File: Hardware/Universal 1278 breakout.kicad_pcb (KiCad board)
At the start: 2 copper layers, 26.7 x 30.6 mm, 7 parts, among them J1 Conn_Coaxial, J2 Conn_01x10, J3 Conn_01x10, U2 DRF1278F

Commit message: Various updates.
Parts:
- J1: footprint Connector_Coaxial:SMA_Molex_73251-2120_EdgeMount_Horizontal -> My footprints:SMA_EdgeMount_Holes
- moved J1 0.07 mm to (155.5, 81.4), turned to 180 degrees
- renumbered XL2178-SMT to U1
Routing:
- net (no net): track 2.54 -> 0.00 mm
- net DIO5: track 46.6 -> 48.1 mm
- net DIO4: track 41.2 -> 42.7 mm
- net RESET: track 36.2 -> 37.3 mm
- net GND: track 17.0 -> 15.9 mm, vias 26 -> 42
- net DIO1: track 30.7 -> 31.4 mm
- net DIO2: track 28.0 -> 28.6 mm
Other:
- board text added: "MBB LoRa DRF1278F/ XL1278-SMT BB v1.0 git.io/JtAfU"
- board text removed: "TODO: * U.FL etc. footprint with holes for ANT * Groundplane * Another set of 0.05" holes to adapt XL1278-SMT to DRF1278F with 0.05" pins?"

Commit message: Update.
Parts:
- J1: footprint My footprints:SMA_EdgeMount_Holes -> Misc RF:SMA_EdgeMount_Holes
- U1: footprint My footprints:XL1278-SMT -> Misc RF:XL1278-SMT
- U2: footprint My footprints:DRF1278F -> Misc RF:DRF1278F
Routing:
- net GND: track 15.9 -> 29.9 mm

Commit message: Further updates
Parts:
- removed JP1: SolderJumper_3_Open, Jumper:SolderJumper-3_P1.3mm_Open_RoundedPad1.0x1.5mm
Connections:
- U1 pad 16: Net-(JP1-Pad3) -> Net-(J1-Pad1)
- U2 pad 15: Net-(JP1-Pad1) -> Net-(J1-Pad1)
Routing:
- net Net-(J1-Pad1): track 15.3 -> 17.5 mm
- net Net-(JP1-Pad1): track 2.02 -> 0.00 mm
- net Net-(JP1-Pad3): track 1.78 -> 0.00 mm
- net DIO0: track 30.1 -> 29.1 mm
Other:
- board text added: "BB v1.0"
- board text removed: "BB v0.1"

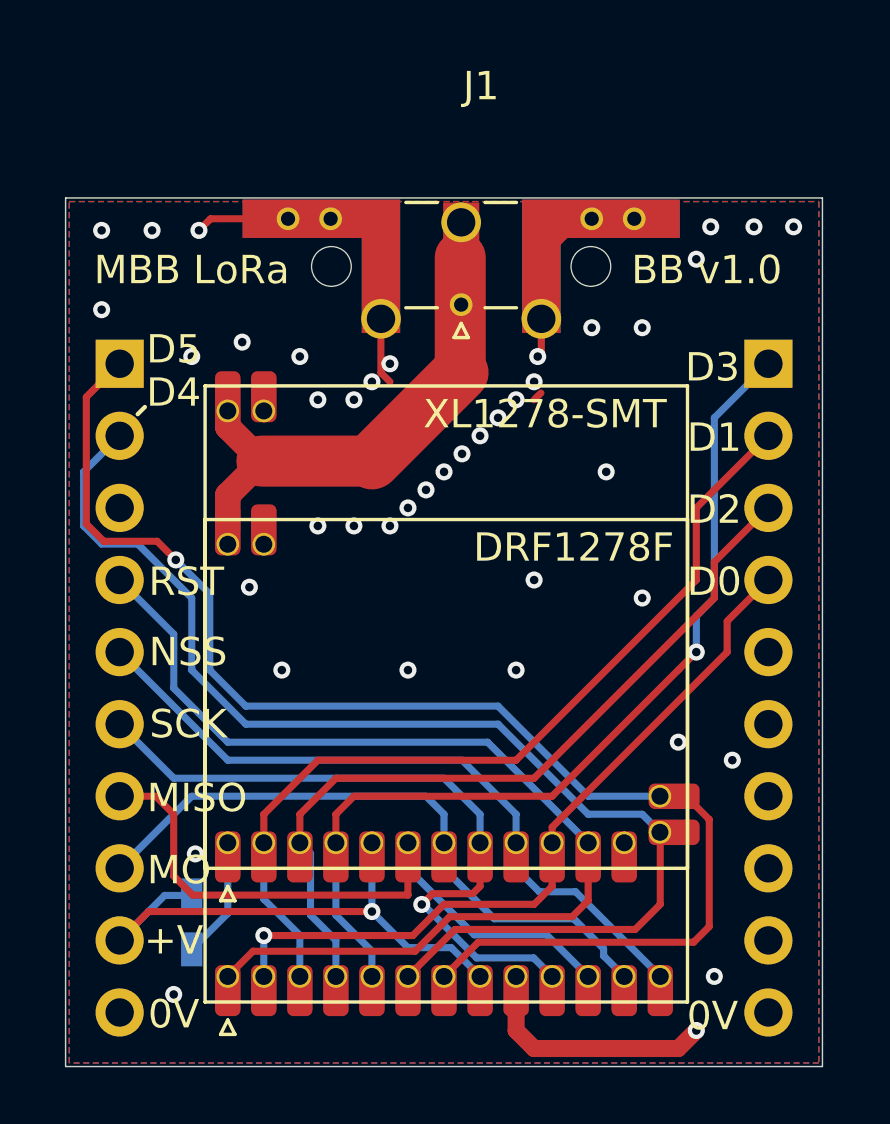
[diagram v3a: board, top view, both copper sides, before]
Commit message: Fix antenna ground connections
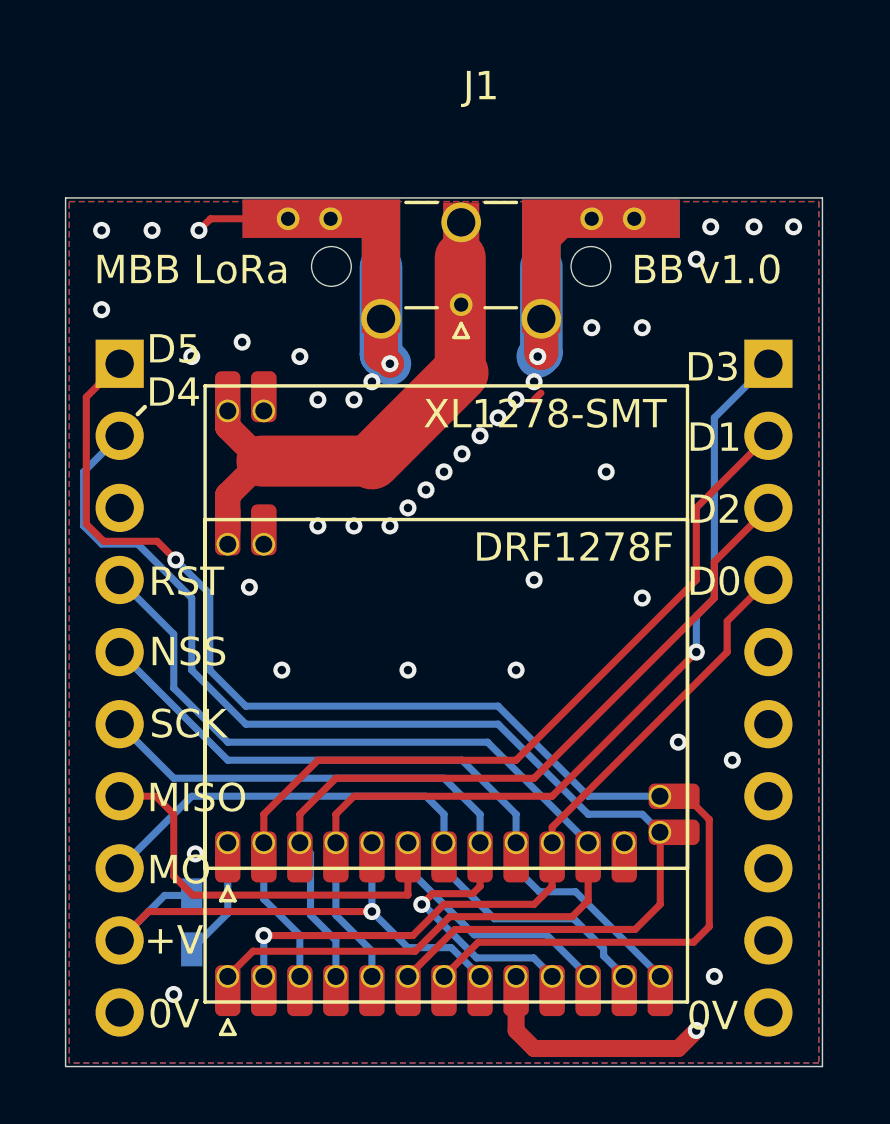
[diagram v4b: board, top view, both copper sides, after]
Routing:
- net GND: track 30.0 -> 36.2 mm
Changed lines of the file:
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@@
     (thickness 1.6002)
     (drawings 28)
-    (tracks 213)
+    (tracks 217)
     (zones 0)
     (modules 6)
@@
   )
   (setup
-    (last_trace_width 0.25)
+    (last_trace_width 1.5)
     (user_trace_width 0.15)
     (user_trace_width 0.2)
@@
     (visible_elements 7FFFFFFF)
     (pcbplotparams
-      (layerselection 0x010fc_ffffffff)
+      (layerselection 0x010f0_ffffffff)
       (usegerberextensions false)
       (usegerberattributes true)
@@
       (drillshape 0)
       (scaleselection 1)
-      (outputdirectory ""))
+      (outputdirectory "Gerbers/"))
   )
   (net 0 "")
@@
       (effects (font (size 1 1) (thickness 0.15)))
     )
-    (fp_text user %R (at 9.095 0 180) (layer F.Fab)
-      (effects (font (size 1 1) (thickness 0.15)))
-    )
-    (fp_text user "PCB Edge" (at 0.127 2.6035 180) (layer Dwgs.User)
-      (effects (font (size 0.5 0.5) (thickness 0.08)))
-    )
-    (fp_text user "Board Thickness: 1.57mm" (at 0 -5.45 180) (layer Cmts.User)
-      (effects (font (size 1 1) (thickness 0.15)))
-    )
     (fp_line (start -0.25 -2.76) (end 0 -2.26) (layer F.SilkS) (width 0.12))
     (fp_line (start 0.25 -2.76) (end -0.25 -2.76) (layer F.SilkS) (width 0.12))
@@
     (fp_line (start -1.95 -1.71) (end -0.84 -1.71) (layer F.SilkS) (width 0.12))
     (fp_line (start 0.84 -1.71) (end 1.95 -1.71) (layer F.SilkS) (width 0.12))
+    (fp_text user %R (at 9.095 0 180) (layer F.Fab)
+      (effects (font (size 1 1) (thickness 0.15)))
+    )
+    (fp_text user "PCB Edge" (at 0.127 2.6035 180) (layer Dwgs.User)
+      (effects (font (size 0.5 0.5) (thickness 0.08)))
+    )
+    (fp_text user "Board Thickness: 1.57mm" (at 0 -5.45 180) (layer Cmts.User)
+      (effects (font (size 1 1) (thickness 0.15)))
+    )
     (pad 2 smd rect (at -5.6 1.425 270) (size 1.35 4.2) (layers Back B.Mask)
       (net 2 GND))
@@
   )
   (segment (start 155.5115 81.3435) (end 155.5115 85.4075) (width 1.8) (layer Front) (net 1))
+  (segment (start 147.32 87.317685) (end 148.521315 88.519) (width 0.9) (layer Front) (net 1))
+  (segment (start 147.32 86.752) (end 147.32 87.317685) (width 0.9) (layer Front) (net 1))
+  (segment (start 147.32 89.720315) (end 147.32 90.943) (width 0.9) (layer Front) (net 1))
+  (segment (start 148.521315 88.519) (end 147.32 89.720315) (width 0.9) (layer Front) (net 1))
+  (segment (start 155.5115 85.4075) (end 152.4 88.519) (width 2) (layer Front) (net 1))
+  (segment (start 152.4 88.519) (end 148.521315 88.519) (width 1.8) (layer Front) (net 1))
   (via (at 163.83 108.585) (size 0.6) (drill 0.3) (layers Front Back) (net 2))
   (via (at 145.415 107.315) (size 0.6) (drill 0.3) (layers Front Back) (net 2))
@@
   (via (at 158.115 92.71) (size 0.6) (drill 0.3) (layers Front Back) (net 2))
   (via (at 153.67 95.885) (size 0.6) (drill 0.3) (layers Front Back) (net 2))
-  (segment (start 152.7048 81.3816) (end 152.7048 83.8708) (width 0.25) (layer Front) (net 2))
+  (segment (start 152.7048 81.3816) (end 152.7048 83.8708) (width 1.2) (layer Front) (net 2))
   (segment (start 158.3548 86.1202) (end 158.115 86.36) (width 0.25) (layer Front) (net 2))
   (via (at 164.338 80.264) (size 0.6) (drill 0.3) (layers Front Back) (net 2))
@@
   (via (at 146.177 102.362) (size 0.6) (drill 0.3) (layers Front Back) (net 2))
   (via (at 148.082 92.964) (size 0.6) (drill 0.3) (layers Front Back) (net 2))
+  (segment (start 158.369 84.709) (end 158.242 84.836) (width 0.25) (layer Front) (net 2))
+  (segment (start 158.369 81.657) (end 158.369 84.709) (width 1.2) (layer Front) (net 2))
+  (segment (start 152.719 84.774) (end 153.035 85.09) (width 1) (layer Front) (net 2))
+  (segment (start 152.719 81.657) (end 152.719 84.774) (width 1.2) (layer Front) (net 2))
+  (segment (start 158.369 84.709) (end 158.242 84.836) (width 1.5) (layer Back) (net 2))
+  (segment (start 158.369 81.657) (end 158.369 84.709) (width 1.5) (layer Back) (net 2))
+  (segment (start 152.719 84.774) (end 153.035 85.09) (width 1.5) (layer Back) (net 2))
+  (segment (start 152.719 81.657) (end 152.719 84.774) (width 1.5) (layer Back) (net 2))
   (segment (start 156.21 106.68) (end 155.194 105.664) (width 0.25) (layer Back) (net 3))
   (segment (start 155.194 105.664) (end 153.67 105.664) (width 0.25) (layer Back) (net 3))
@@
   (segment (start 148.59 103.955998) (end 149.86 105.225998) (width 0.25) (layer Back) (net 13))
   (segment (start 148.59 101.97) (end 148.59 103.955998) (width 0.25) (layer Back) (net 13))
+  (segment (start 163.83 92.71) (end 163.83 90.17) (width 0.25) (layer Front) (net 13))
+  (segment (start 157.48 99.06) (end 163.83 92.71) (width 0.25) (layer Front) (net 13))
+  (segment (start 150.495 99.06) (end 157.48 99.06) (width 0.25) (layer Front) (net 13))
+  (segment (start 148.59 100.965) (end 150.495 99.06) (width 0.25) (layer Front) (net 13))
+  (segment (start 148.59 101.97) (end 148.59 100.965) (width 0.25) (layer Front) (net 13))
+  (segment (start 163.83 90.17) (end 166.37 87.63) (width 0.25) (layer Front) (net 13))
   (segment (start 165.735 90.17) (end 166.37 90.17) (width 0.25) (layer Front) (net 14))
   (segment (start 150.237009 102.347009) (end 150.237009 104.517009) (width 0.25) (layer Back) (net 14))
@@
   (segment (start 164.918038 94.161962) (end 166.37 92.71) (width 0.25) (layer Front) (net 15))
   (segment (start 164.918038 95.25) (end 164.918038 94.161962) (width 0.25) (layer Front) (net 15))
-  (segment (start 147.32 87.317685) (end 148.521315 88.519) (width 0.9) (layer Front) (net 1))
-  (segment (start 147.32 86.752) (end 147.32 87.317685) (width 0.9) (layer Front) (net 1))
-  (segment (start 147.32 89.720315) (end 147.32 90.943) (width 0.9) (layer Front) (net 1))
-  (segment (start 148.521315 88.519) (end 147.32 89.720315) (width 0.9) (layer Front) (net 1))
-  (segment (start 155.5115 85.4075) (end 152.4 88.519) (width 2) (layer Front) (net 1))
-  (segment (start 152.4 88.519) (end 148.521315 88.519) (width 1.8) (layer Front) (net 1))
-  (segment (start 152.719 85.409) (end 153.035 85.725) (width 0.25) (layer Front) (net 2))
-  (segment (start 152.719 81.657) (end 152.719 85.409) (width 0.25) (layer Front) (net 2))
-  (segment (start 158.369 84.709) (end 158.242 84.836) (width 0.25) (layer Front) (net 2))
-  (segment (start 158.369 81.657) (end 158.369 84.709) (width 0.25) (layer Front) (net 2))
-  (segment (start 163.83 92.71) (end 163.83 90.17) (width 0.25) (layer Front) (net 13))
-  (segment (start 157.48 99.06) (end 163.83 92.71) (width 0.25) (layer Front) (net 13))
-  (segment (start 150.495 99.06) (end 157.48 99.06) (width 0.25) (layer Front) (net 13))
-  (segment (start 148.59 100.965) (end 150.495 99.06) (width 0.25) (layer Front) (net 13))
-  (segment (start 148.59 101.97) (end 148.59 100.965) (width 0.25) (layer Front) (net 13))
-  (segment (start 163.83 90.17) (end 166.37 87.63) (width 0.25) (layer Front) (net 13))
   (zone (net 2) (net_name GND) (layer Back) (hatch edge 0.508)
     (connect_pads (clearance 0.508))
@@
     (polygon
       (pts
-        (xy 157.48 84.455) (xy 153.543 84.455) (xy 153.543 79.375) (xy 157.4798 79.3816)
+        (xy 157.48 85.09) (xy 153.543 85.09) (xy 153.543 79.375) (xy 157.4798 79.3816)
       )
     )

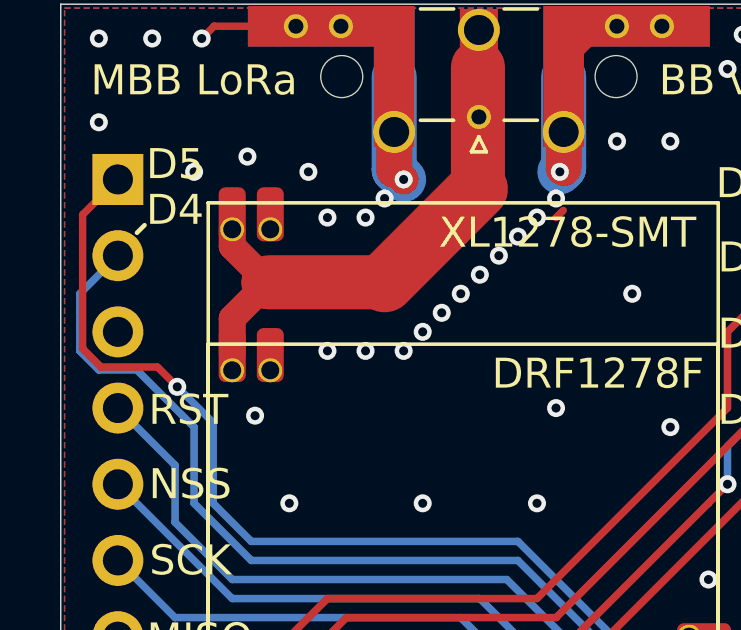
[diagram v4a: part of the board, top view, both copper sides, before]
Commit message: Fix more grounds.
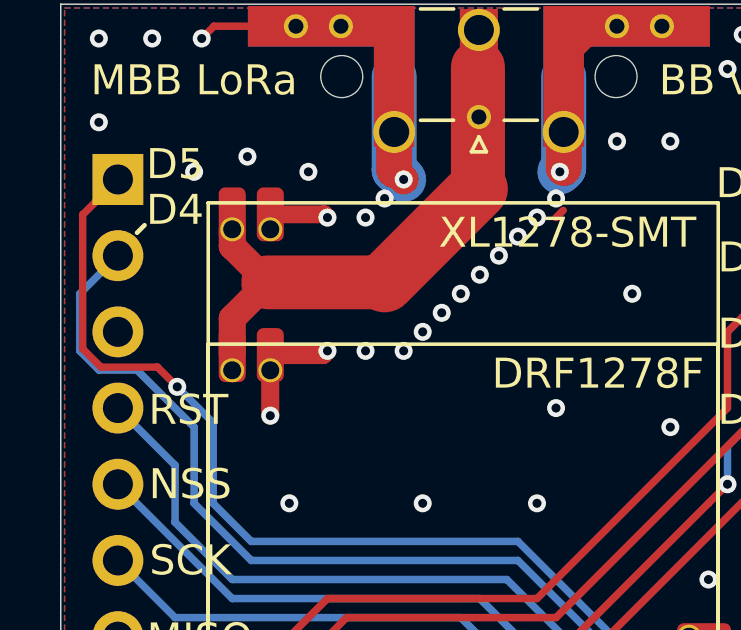
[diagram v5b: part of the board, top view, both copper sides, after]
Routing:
- net GND: track 36.2 -> 42.1 mm
